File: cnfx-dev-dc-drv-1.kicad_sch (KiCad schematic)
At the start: 55 parts, among them J1 TC2030, J2 Conn_01x02, J3 Conn_01x04_Pin, J4 Conn_01x02, J7 Conn_01x03, J8 Conn_01x04_Pin, SW1 SW_Push, SW2 SW_Push, SW3 SW_Push, U1 SN65HVD230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

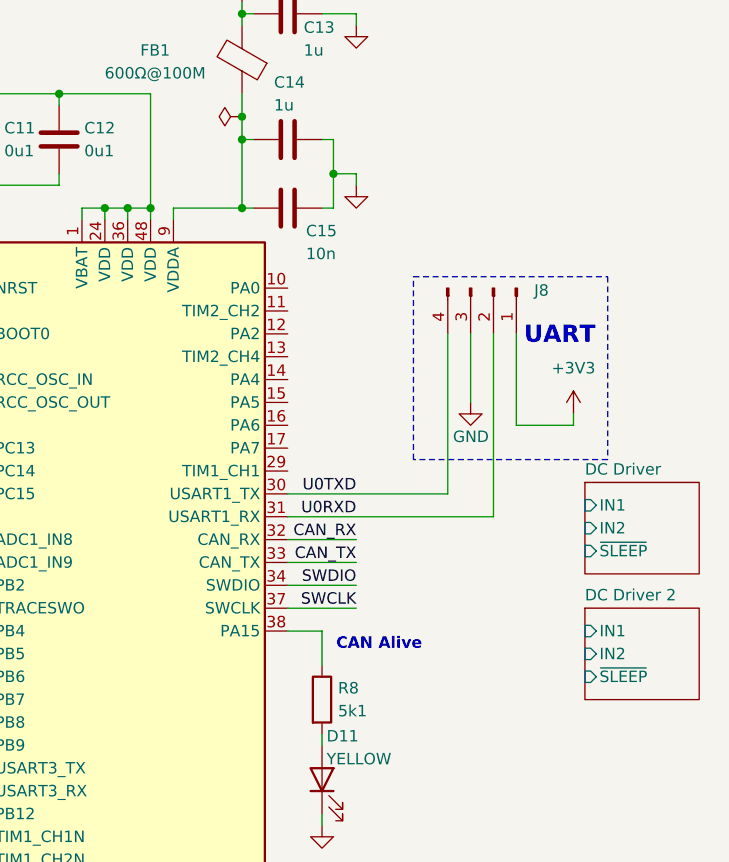
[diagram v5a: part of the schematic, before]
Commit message: schem: connect DC drivers to stm32
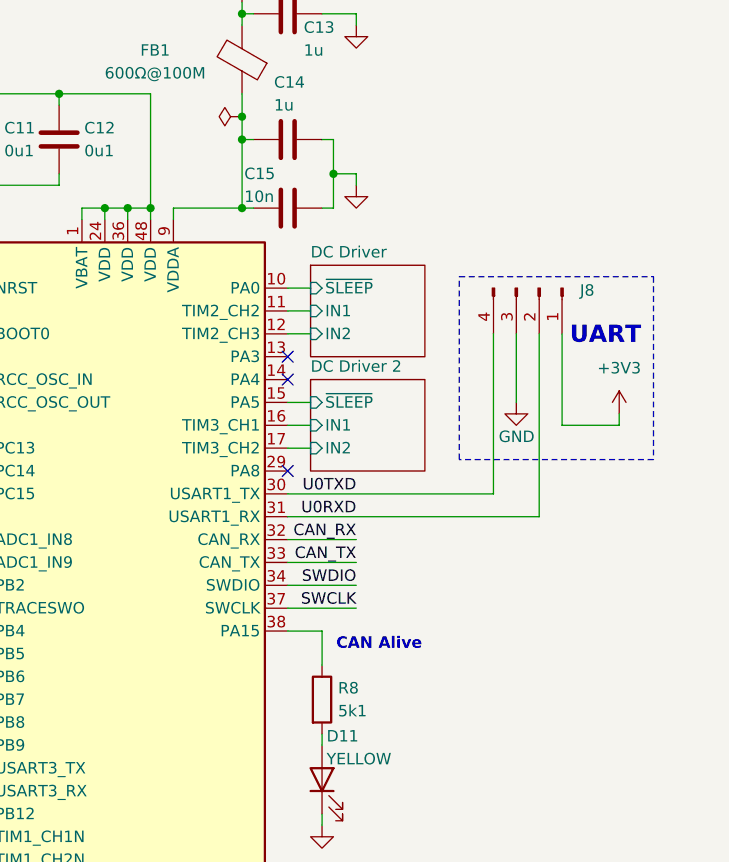
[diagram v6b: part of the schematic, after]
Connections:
- net DC Driver 2/IN1: now also U2.16 (PA6)
- net DC Driver 2/IN2: now also U2.17 (PA7)
- net DC Driver 2/~{SLEEP}: now also U2.15 (PA5)
- net DC Driver/IN1: now also U2.11 (PA1)
- net DC Driver/IN2: now also U2.12 (PA2)
- net DC Driver/~{SLEEP}: now also U2.10 (PA0)
- no-connect marks 13 -> 16
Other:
- moved on the sheet: J8
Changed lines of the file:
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@@
 	(paper "A4")
 	(rectangle
-		(start 184.15 71.12)
-		(end 205.74 91.44)
+		(start 189.23 71.12)
+		(end 210.82 91.44)
 		(stroke
 			(width 0)
@@
 	(text "UART"
 		(exclude_from_sim no)
-		(at 200.406 77.724 0)
+		(at 205.486 77.724 0)
 		(effects
 			(font
@@
 	)
 	(no_connect
+		(at 170.18 80.01)
+	)
+	(no_connect
 		(at 134.62 100.33)
 	)
@@
 	)
 	(no_connect
+		(at 170.18 92.71)
+	)
+	(no_connect
 		(at 134.62 92.71)
 	)
 	(no_connect
+		(at 170.18 82.55)
+	)
+	(no_connect
 		(at 134.62 115.57)
 	)
@@
 	(wire
 		(pts
+			(xy 170.18 74.93) (xy 172.72 74.93)
+		)
+		(stroke
+			(width 0)
+			(type default)
+		)
+	)
+	(wire
+		(pts
 			(xy 36.83 101.6) (xy 36.83 99.06)
 		)
@@
 	(wire
 		(pts
+			(xy 170.18 97.79) (xy 198.12 97.79)
+		)
+		(stroke
+			(width 0)
+			(type default)
+		)
+	)
+	(wire
+		(pts
 			(xy 86.36 148.59) (xy 86.36 149.86)
 		)
@@
 	(wire
 		(pts
-			(xy 190.5 77.47) (xy 190.5 85.09)
+			(xy 195.58 77.47) (xy 195.58 85.09)
 		)
 		(stroke
@@
 	(wire
 		(pts
-			(xy 67.31 173.99) (xy 85.09 173.99)
+			(xy 170.18 85.09) (xy 172.72 85.09)
 		)
 		(stroke
@@
 	(wire
 		(pts
-			(xy 152.4 147.32) (xy 152.4 146.05)
+			(xy 67.31 173.99) (xy 85.09 173.99)
 		)
 		(stroke
@@
 	(wire
 		(pts
-			(xy 97.79 189.23) (xy 97.79 187.96)
+			(xy 152.4 147.32) (xy 152.4 146.05)
 		)
 		(stroke
@@
 	(wire
 		(pts
-			(xy 151.13 167.64) (xy 144.78 167.64)
+			(xy 97.79 189.23) (xy 97.79 187.96)
 		)
 		(stroke
@@
 	(wire
 		(pts
-			(xy 170.18 97.79) (xy 193.04 97.79)
+			(xy 151.13 167.64) (xy 144.78 167.64)
 		)
 		(stroke
@@
 	(wire
 		(pts
-			(xy 201.93 86.36) (xy 201.93 87.63)
+			(xy 207.01 86.36) (xy 207.01 87.63)
 		)
 		(stroke
@@
 	(wire
 		(pts
-			(xy 195.58 87.63) (xy 195.58 77.47)
+			(xy 200.66 87.63) (xy 200.66 77.47)
 		)
 		(stroke
@@
 	(wire
 		(pts
+			(xy 170.18 95.25) (xy 193.04 95.25)
+		)
+		(stroke
+			(width 0)
+			(type default)
+		)
+	)
+	(wire
+		(pts
+			(xy 170.18 72.39) (xy 172.72 72.39)
+		)
+		(stroke
+			(width 0)
+			(type default)
+		)
+	)
+	(wire
+		(pts
 			(xy 57.15 161.29) (xy 57.15 162.56)
 		)
@@
 	(wire
 		(pts
-			(xy 193.04 77.47) (xy 193.04 97.79)
+			(xy 198.12 77.47) (xy 198.12 97.79)
 		)
 		(stroke
@@
 	(wire
 		(pts
-			(xy 201.93 87.63) (xy 195.58 87.63)
+			(xy 207.01 87.63) (xy 200.66 87.63)
 		)
 		(stroke
@@
 	(wire
 		(pts
-			(xy 187.96 77.47) (xy 187.96 95.25)
+			(xy 193.04 77.47) (xy 193.04 95.25)
 		)
 		(stroke
@@
 	(wire
 		(pts
+			(xy 170.18 90.17) (xy 172.72 90.17)
+		)
+		(stroke
+			(width 0)
+			(type default)
+		)
+	)
+	(wire
+		(pts
 			(xy 52.07 104.14) (xy 52.07 105.41)
 		)
@@
 	(wire
 		(pts
+			(xy 170.18 87.63) (xy 172.72 87.63)
+		)
+		(stroke
+			(width 0)
+			(type default)
+		)
+	)
+	(wire
+		(pts
 			(xy 151.13 170.18) (xy 151.13 167.64)
 		)
@@
 	(wire
 		(pts
-			(xy 170.18 95.25) (xy 187.96 95.25)
-		)
-		(stroke
-			(width 0)
-			(type default)
-		)
-	)
-	(wire
-		(pts
 			(xy 19.05 151.13) (xy 24.13 151.13)
 		)
@@
 	(wire
 		(pts
+			(xy 170.18 77.47) (xy 172.72 77.47)
+		)
+		(stroke
+			(width 0)
+			(type default)
+		)
+	)
+	(wire
+		(pts
 			(xy 132.08 72.39) (xy 128.27 72.39)
 		)
@@
 		)
 		(pin "12"
+			(alternate "TIM2_CH3")
 		)
 		(pin "13"
-			(alternate "TIM2_CH4")
 		)
 		(pin "1"
@@
 		)
 		(pin "29"
-			(alternate "TIM1_CH1")
 		)
 		(pin "38"
@@
 		)
 		(pin "17"
+			(alternate "TIM3_CH2")
 		)
 		(pin "25"
 		)
 		(pin "16"
+			(alternate "TIM3_CH1")
 		)
 		(pin "9"
@@
 	(symbol
 		(lib_id "power:GND")
-		(at 190.5 85.09 0)
+		(at 195.58 85.09 0)
 		(unit 1)
 		(body_style 1)
@@
 		(dnp no)
 		(property "Reference" "#PWR049"
-			(at 190.5 91.44 0)
+			(at 195.58 91.44 0)
 			(hide yes)
 			(show_name no)
@@
 		)
 		(property "Value" "GND"
-			(at 192.532 88.9 0)
+			(at 197.612 88.9 0)
 			(show_name no)
 			(do_not_autoplace no)
@@
 		)
 		(property "Footprint" ""
-			(at 190.5 85.09 0)
+			(at 195.58 85.09 0)
 			(hide yes)
 			(show_name no)
@@
 		)
 		(property "Datasheet" ""
-			(at 190.5 85.09 0)
+			(at 195.58 85.09 0)
 			(hide yes)
 			(show_name no)
@@
 		)
 		(property "Description" "Power symbol creates a global label with name \"GND\" , ground"
-			(at 190.5 85.09 0)
+			(at 195.58 85.09 0)
 			(hide yes)
 			(show_name no)
@@
 	(symbol
 		(lib_id "power:+3V3")
-		(at 201.93 86.36 0)
+		(at 207.01 86.36 0)
 		(unit 1)
 		(body_style 1)
@@
 		(fields_autoplaced yes)
 		(property "Reference" "#PWR050"
-			(at 201.93 90.17 0)
+			(at 207.01 90.17 0)
 			(hide yes)
 			(show_name no)
@@
 		)
 		(property "Value" "+3V3"
-			(at 201.93 81.28 0)
+			(at 207.01 81.28 0)
 			(show_name no)
 			(do_not_autoplace no)
@@
 		)
 		(property "Footprint" ""
-			(at 201.93 86.36 0)
+			(at 207.01 86.36 0)
 			(hide yes)
 			(show_name no)
@@
 		)
 		(property "Datasheet" ""
-			(at 201.93 86.36 0)
+			(at 207.01 86.36 0)
 			(hide yes)
 			(show_name no)
@@
 		)
 		(property "Description" "Power symbol creates a global label with name \"+3V3\""
-			(at 201.93 86.36 0)
+			(at 207.01 86.36 0)
 			(hide yes)
 			(show_name no)
@@
 	(symbol
 		(lib_id "Connector:Conn_01x04_Pin")
-		(at 193.04 72.39 270)
+		(at 198.12 72.39 270)
 		(unit 1)
 		(body_style 1)
@@
 		(dnp no)
 		(property "Reference" "J8"
-			(at 198.374 72.644 90)
+			(at 203.454 72.644 90)
 			(show_name no)
 			(do_not_autoplace no)
@@
 		)
 		(property "Value" "Conn_01x04_Pin"
-			(at 191.77 69.85 90)
+			(at 196.85 69.85 90)
 			(hide yes)
 			(show_name no)
@@
 		)
 		(property "Footprint" "Connector_PinHeader_2.54mm:PinHeader_1x04_P2.54mm_Vertical"
-			(at 193.04 72.39 0)
+			(at 198.12 72.39 0)
 			(hide yes)
 			(show_name no)
@@
 		)
 		(property "Datasheet" ""
-			(at 193.04 72.39 0)
+			(at 198.12 72.39 0)
 			(hide yes)
 			(show_name no)
@@
 		)
 		(property "Description" "Generic connector, single row, 01x04, script generated"
-			(at 193.04 72.39 0)
+			(at 198.12 72.39 0)
 			(hide yes)
 			(show_name no)
@@
 		(dnp no)
 		(property "Reference" "C15"
-			(at 172.212 66.04 90)
+			(at 165.354 59.69 90)
 			(show_name no)
 			(do_not_autoplace no)
@@
 		)
 		(property "Value" "10n"
-			(at 172.212 68.58 90)
+			(at 165.354 62.23 90)
 			(show_name no)
 			(do_not_autoplace no)
@@
 	)
 	(sheet
-		(at 203.2 107.95)
+		(at 172.72 82.55)
 		(size 12.7 10.16)
 		(exclude_from_sim no)
@@
 		)
 		(property "Sheetname" "DC Driver 2"
-			(at 203.2 107.2384 0)
+			(at 172.72 81.8384 0)
 			(show_name no)
 			(do_not_autoplace no)
@@
 		)
 		(property "Sheetfile" "dc-drv.kicad_sch"
-			(at 203.2 118.6946 0)
+			(at 172.72 93.2946 0)
 			(hide yes)
 			(show_name no)
@@
 		)
 		(pin "~{SLEEP}" input
-			(at 203.2 115.57 180)
+			(at 172.72 85.09 180)
 			(effects
 				(font
@@
 		)
 		(pin "IN1" input
-			(at 203.2 110.49 180)
+			(at 172.72 87.63 180)
 			(effects
 				(font
@@
 		)
 		(pin "IN2" input
-			(at 203.2 113.03 180)
+			(at 172.72 90.17 180)
 			(effects
 				(font
@@
 	)
 	(sheet
-		(at 203.2 93.98)
+		(at 172.72 69.85)
 		(size 12.7 10.16)
 		(exclude_from_sim no)
@@
 		)
 		(property "Sheetname" "DC Driver"
-			(at 203.2 93.2684 0)
+			(at 172.72 69.1384 0)
 			(show_name no)
 			(do_not_autoplace no)
@@
 		)
 		(property "Sheetfile" "dc-drv.kicad_sch"
-			(at 203.2 104.7246 0)
+			(at 172.72 80.5946 0)
 			(hide yes)
 			(show_name no)
@@
 		)
 		(pin "~{SLEEP}" input
-			(at 203.2 101.6 180)
+			(at 172.72 72.39 180)
 			(effects
 				(font
@@
 		)
 		(pin "IN1" input
-			(at 203.2 96.52 180)
+			(at 172.72 74.93 180)
 			(effects
 				(font
@@
 		)
 		(pin "IN2" input
-			(at 203.2 99.06 180)
+			(at 172.72 77.47 180)
 			(effects
 				(font
